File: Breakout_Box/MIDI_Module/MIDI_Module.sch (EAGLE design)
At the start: 71 parts, among them T1 2N2222, T2 2N2222, U1 TLV6004, U2 TLV6004, U3 MIC5205-5.0YM5-TR, U4 MIC5205-3.3YM5-TR

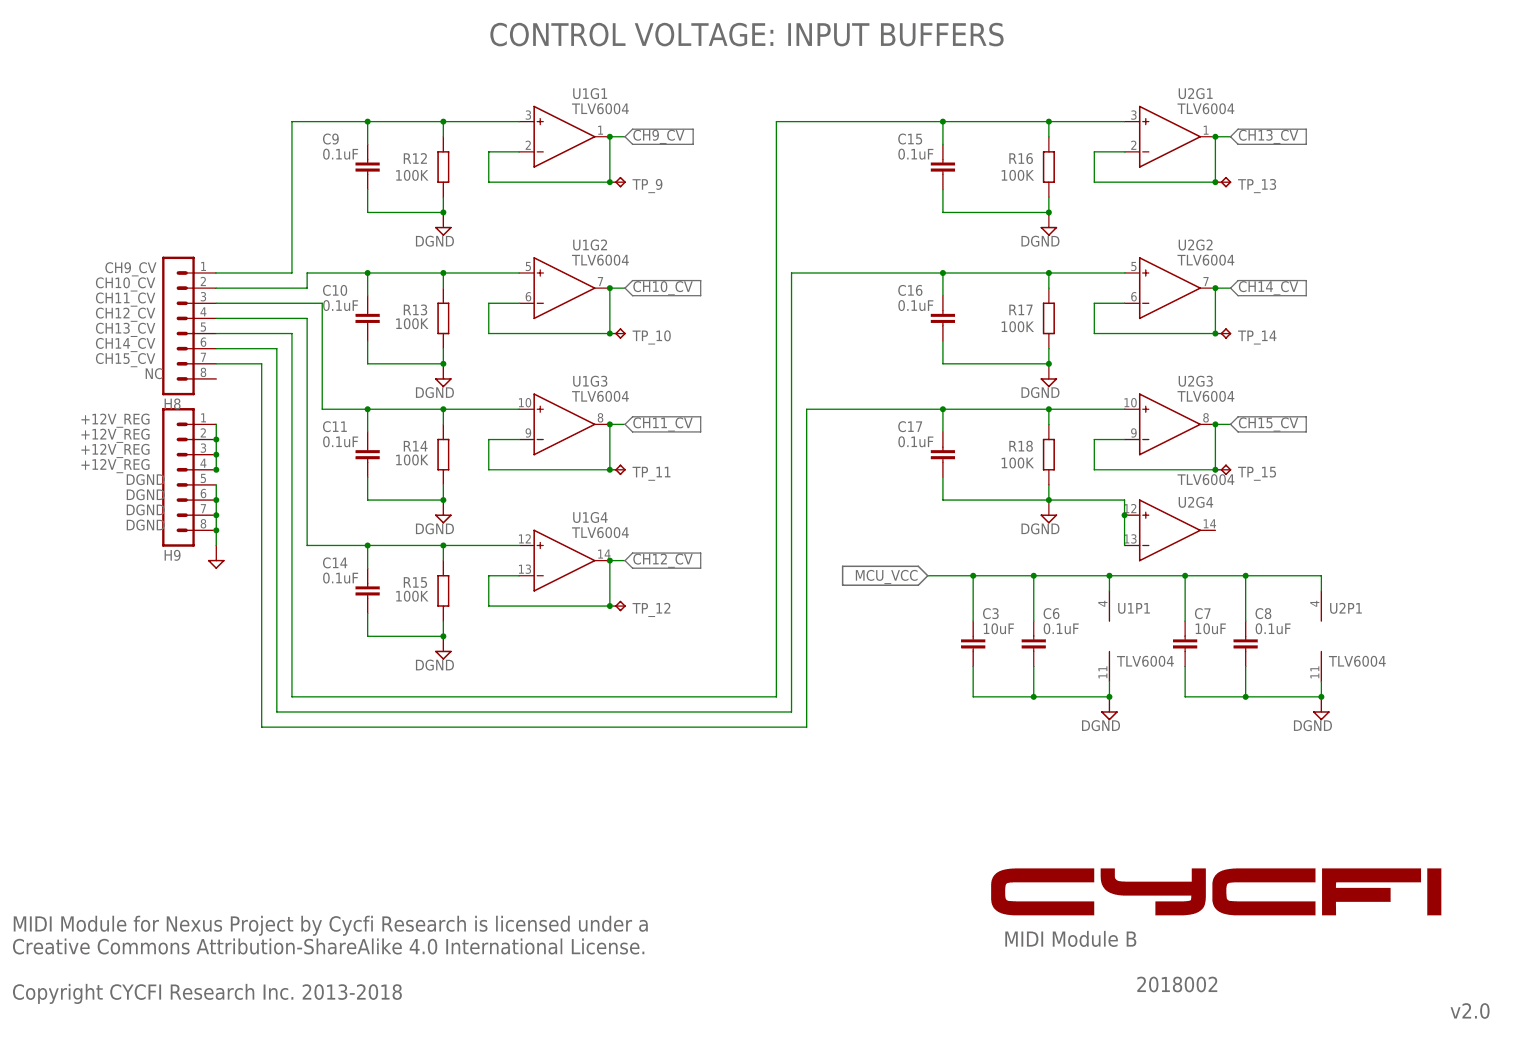
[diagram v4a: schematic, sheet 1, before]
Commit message: Update: Main Board MIDI Board MCU Board IO Board
Delete:
Mixer Board
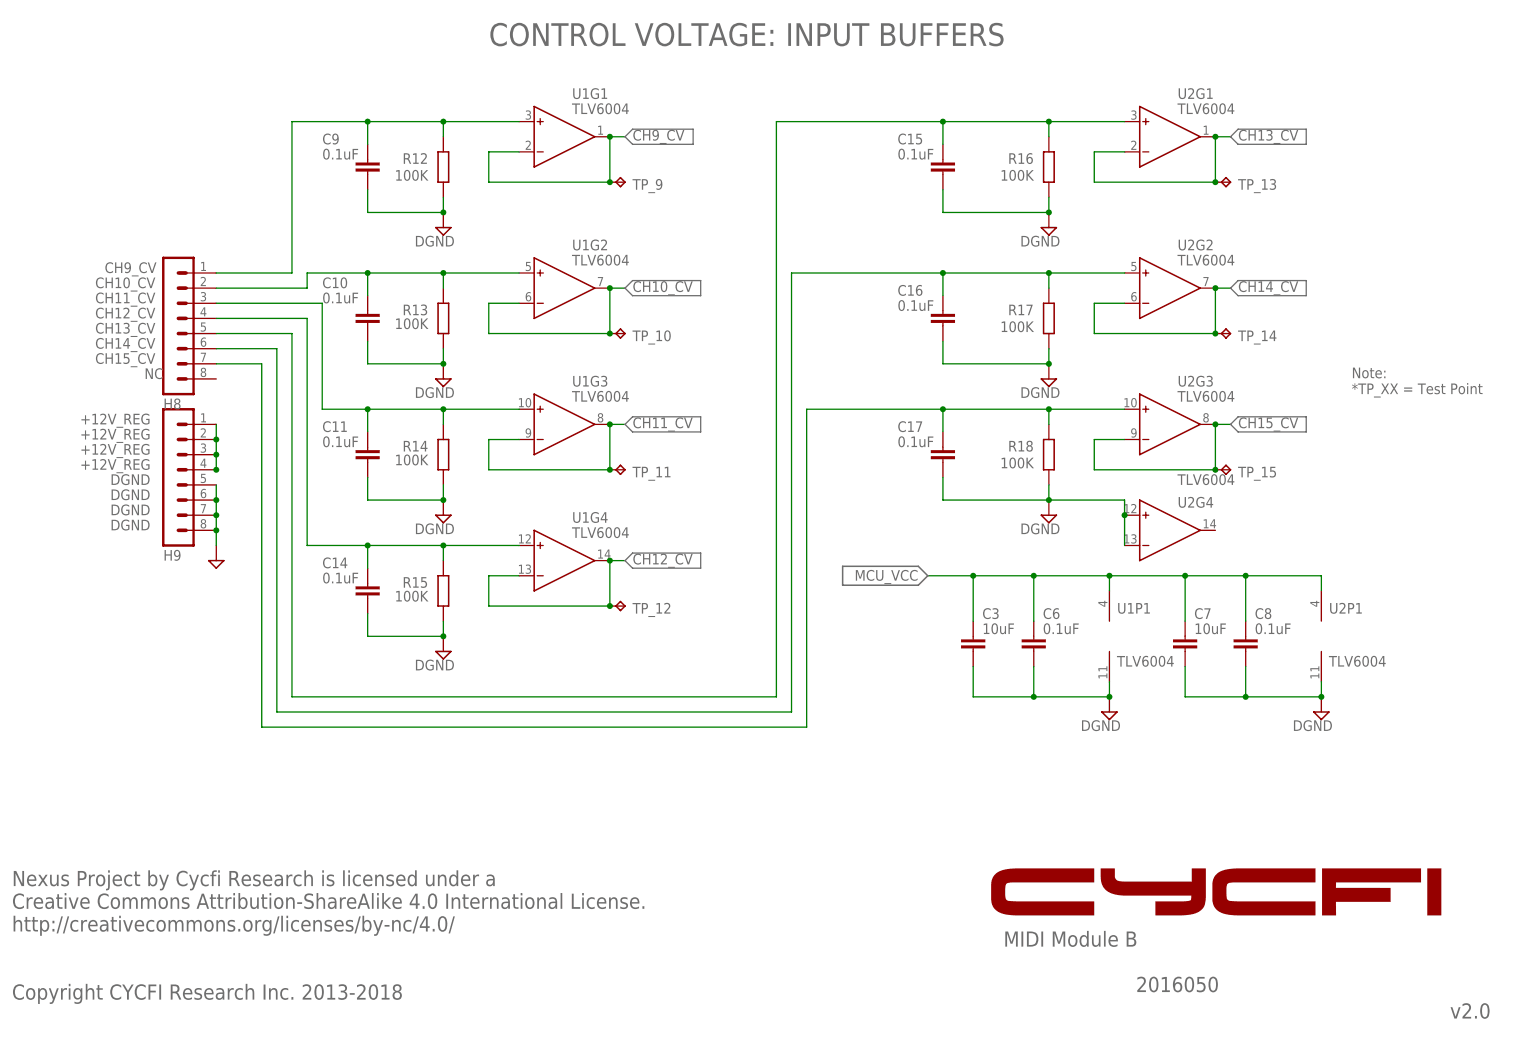
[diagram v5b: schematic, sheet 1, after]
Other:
- note added: "2016050"
- note added: "Nexus Project by Cycfi Research is licensed under a Creative Commons Attribution-ShareAlike 4.0 International License. http://creativecommons.org/licenses/by-nc/4.0/ Copyright CYCFI Research Inc. 2013-2018"
- note added: "Note: *TP_XX = Test Point"
- note removed: "2018002"
- note removed: "MIDI Module for Nexus Project by Cycfi Research is licensed under a Creative Commons Attribution-ShareAlike 4.0 International License. Copyright CYCFI Research Inc. 2013-2018"
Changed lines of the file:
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@@
 <setting verticaltext="up"/>
 </settings>
-<grid distance="0.1" unitdist="inch" unit="inch" style="lines" multiple="1" display="no" altdistance="0.01" altunitdist="inch" altunit="inch"/>
+<grid distance="0.05" unitdist="inch" unit="inch" style="lines" multiple="1" display="no" altdistance="0.01" altunitdist="inch" altunit="inch"/>
 <layers>
 <layer number="1" name="Top" color="4" fill="1" visible="no" active="no"/>
@@
 <text x="177.8" y="19.05" size="2.54" layer="95">MIDI Module B</text>
 <text x="252.73" y="6.985" size="2.54" layer="95">v2.0</text>
-<text x="200.025" y="11.43" size="2.54" layer="95">2018002</text>
+<text x="200.025" y="11.43" size="2.54" layer="95">2016050</text>
 <wire x1="150.8125" y1="82.8675" x2="150.8125" y2="79.6925" width="0.254" layer="95"/>
 <wire x1="150.8125" y1="79.6925" x2="163.5125" y2="79.6925" width="0.254" layer="95"/>
@@
 <text x="25.4" y="119.38" size="1.778" layer="95">CH14_CV</text>
 <text x="25.4" y="116.84" size="1.778" layer="95">CH15_CV</text>
-<text x="30.48" y="91.44" size="1.778" layer="95">DGND</text>
+<text x="27.94" y="91.44" size="1.778" layer="95">DGND</text>
 <text x="33.655" y="114.3" size="1.778" layer="95">NC</text>
 <wire x1="114.3" y1="154.94" x2="115.57" y2="153.67" width="0.1524" layer="95"/>
@@
 <wire x1="217.17" y1="156.21" x2="215.9" y2="154.94" width="0.1524" layer="95"/>
 <text x="91.44" y="170.18" size="3.81" layer="95">CONTROL VOLTAGE: INPUT BUFFERS</text>
-<text x="30.48" y="93.98" size="1.778" layer="95">DGND</text>
-<text x="30.48" y="96.52" size="1.778" layer="95">DGND</text>
-<text x="11.43" y="10.16" size="2.54" layer="95">MIDI Module for Nexus Project by Cycfi Research is licensed under a
+<text x="27.94" y="93.98" size="1.778" layer="95">DGND</text>
+<text x="27.94" y="96.52" size="1.778" layer="95">DGND</text>
+<text x="11.43" y="10.16" size="2.54" layer="95">Nexus Project by Cycfi Research is licensed under a
 Creative Commons Attribution-ShareAlike 4.0 International License.
+http://creativecommons.org/licenses/by-nc/4.0/
 Copyright CYCFI Research Inc. 2013-2018</text>
 <rectangle x1="179.80469375" y1="24.29065625" x2="193.0330125" y2="24.29954375" layer="94"/>
@@
 <rectangle x1="231.251125" y1="32.176084375" x2="247.86653125" y2="32.184971875" layer="94"/>
 <rectangle x1="248.915553125" y1="32.176084375" x2="251.271403125" y2="32.184971875" layer="94"/>
+<text x="236.22" y="111.76" size="1.778" layer="95">Note:
+*TP_XX = Test Point</text>
 </plain>
 <instances>
@@
 </instance>
 <instance part="C10" gate="G$1" x="71.12" y="125.73" smashed="yes">
-<attribute name="NAME" x="63.5" y="128.27" size="1.778" layer="95"/>
-<attribute name="VALUE" x="63.5" y="125.73" size="1.778" layer="96"/>
+<attribute name="NAME" x="63.5" y="129.54" size="1.778" layer="95"/>
+<attribute name="VALUE" x="63.5" y="127" size="1.778" layer="96"/>
 </instance>
 <instance part="C11" gate="G$1" x="71.12" y="102.87" smashed="yes">
@@
 <pinref part="H9" gate="1" pin="7"/>
 <wire x1="45.72" y1="91.44" x2="45.72" y2="88.9" width="0.1524" layer="91"/>
-<label x="30.48" y="88.9" size="1.778" layer="95"/>
+<label x="27.94" y="88.9" size="1.778" layer="95"/>
 <junction x="45.72" y="91.44"/>
 <pinref part="H9" gate="1" pin="5"/>
@@
 <text x="177.8" y="19.05" size="2.54" layer="95">MIDI Module A</text>
 <text x="252.73" y="6.985" size="2.54" layer="95">v2.0</text>
-<text x="200.025" y="11.43" size="2.54" layer="95">2018002</text>
+<text x="200.025" y="11.43" size="2.54" layer="95">2016050</text>
 <text x="142.24" y="122.555" size="1.778" layer="95" rot="MR0">P3.3</text>
 <text x="142.24" y="120.015" size="1.778" layer="95" rot="MR0">P3.2</text>
@@
 <wire x1="230.505" y1="96.52" x2="231.775" y2="96.52" width="0.1524" layer="94"/>
 <wire x1="214.63" y1="180.34" x2="214.63" y2="35.56" width="0.1524" layer="94" style="longdash"/>
-<text x="12.7" y="5.08" size="2.54" layer="95">MIDI Module for Nexus Project by Cycfi Research is licensed under a
+<text x="12.7" y="5.08" size="2.54" layer="95">Nexus Project by Cycfi Research is licensed under a
 Creative Commons Attribution-ShareAlike 4.0 International License.
+http://creativecommons.org/licenses/by-nc/4.0/
 Copyright CYCFI Research Inc. 2013-2018</text>
 <rectangle x1="179.80469375" y1="24.29065625" x2="193.0330125" y2="24.29954375" layer="94"/>
@@
 <wire x1="161.925" y1="143.51" x2="174.3075" y2="143.51" width="0.254" layer="95"/>
 <wire x1="174.3075" y1="143.51" x2="175.895" y2="145.0975" width="0.254" layer="95"/>
-<text x="200.025" y="11.43" size="2.54" layer="95">2018002</text>
+<text x="200.025" y="11.43" size="2.54" layer="95">2016050</text>
 <wire x1="172.085" y1="101.2825" x2="170.4975" y2="102.87" width="0.254" layer="95"/>
 <wire x1="170.4975" y1="102.87" x2="161.925" y2="102.87" width="0.254" layer="95"/>
@@
 <wire x1="86.36" y1="142.875" x2="101.6" y2="142.875" width="0.2032" layer="95"/>
 <wire x1="101.6" y1="142.875" x2="103.505" y2="144.78" width="0.2032" layer="95"/>
-<text x="12.7" y="16.51" size="2.54" layer="95">MIDI Module for Nexus Project by Cycfi Research is licensed under a
+<text x="12.7" y="16.51" size="2.54" layer="95">Nexus Project by Cycfi Research is licensed under a
 Creative Commons Attribution-ShareAlike 4.0 International License.
+http://creativecommons.org/licenses/by-nc/4.0/
 Copyright CYCFI Research Inc. 2013-2018</text>
 <rectangle x1="179.80469375" y1="24.29065625" x2="193.0330125" y2="24.29954375" layer="94"/>

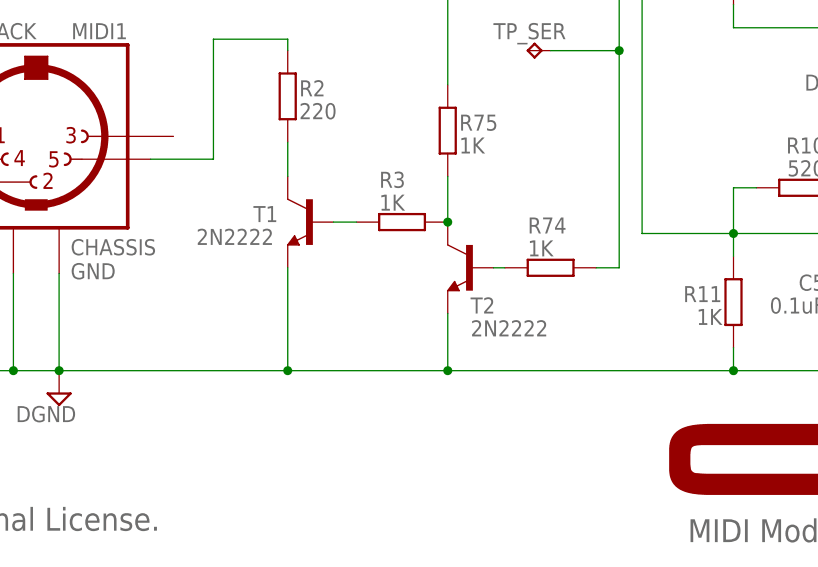
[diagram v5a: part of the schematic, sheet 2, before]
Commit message: Slight Changes to MIDI and MCU: - Change BJT Part number on MIDI_Module - Delete Ferrite Bead on MCU_Module
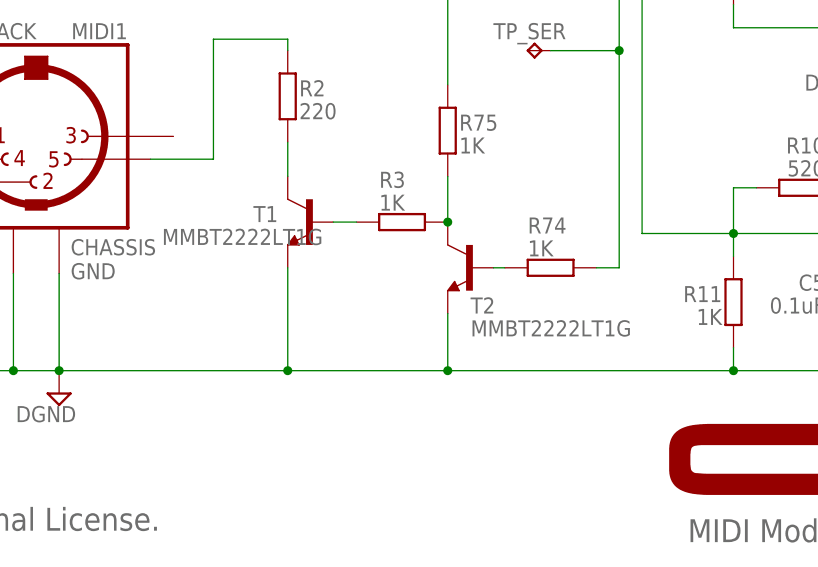
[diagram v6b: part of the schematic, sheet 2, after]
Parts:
- T1, T2: value 2N2222 -> MMBT2222LT1G
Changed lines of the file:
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@@
 <parts>
 <part name="FRAME1" library="frames" library_urn="urn:adsk.eagle:library:229" deviceset="DINA4_L" device=""/>
-<part name="T1" library="Cycfi" deviceset="TRAN-MMBT2222A" device="" value="2N2222"/>
+<part name="T1" library="Cycfi" deviceset="TRAN-MMBT2222A" device="" value="MMBT2222LT1G"/>
 <part name="R3" library="resistor" library_urn="urn:adsk.eagle:library:348" deviceset="R-EU_" device="R0402" package3d_urn="urn:adsk.eagle:package:26058/1" value="1K"/>
 <part name="R2" library="resistor" library_urn="urn:adsk.eagle:library:348" deviceset="R-EU_" device="R0402" package3d_urn="urn:adsk.eagle:package:26058/1" value="220"/>
@@
 <part name="C23" library="resistor" library_urn="urn:adsk.eagle:library:348" deviceset="C-EU" device="C0603" package3d_urn="urn:adsk.eagle:package:26138/1" value="0.1uF"/>
 <part name="C24" library="resistor" library_urn="urn:adsk.eagle:library:348" deviceset="C-EU" device="C0603" package3d_urn="urn:adsk.eagle:package:26138/1" value="0.1uF"/>
-<part name="T2" library="Cycfi" deviceset="TRAN-MMBT2222A" device="" value="2N2222"/>
+<part name="T2" library="Cycfi" deviceset="TRAN-MMBT2222A" device="" value="MMBT2222LT1G"/>
 <part name="R74" library="resistor" library_urn="urn:adsk.eagle:library:348" deviceset="R-EU_" device="R0402" package3d_urn="urn:adsk.eagle:package:26058/1" value="1K"/>
 <part name="R75" library="resistor" library_urn="urn:adsk.eagle:library:348" deviceset="R-EU_" device="R0402" package3d_urn="urn:adsk.eagle:package:26058/1" value="1K"/>
@@
 <instance part="T1" gate="G$1" x="135.89" y="54.61" smashed="yes" rot="MR0">
 <attribute name="NAME" x="129.54" y="54.61" size="1.778" layer="95"/>
-<attribute name="VALUE" x="123.19" y="52.07" size="1.778" layer="96"/>
+<attribute name="VALUE" x="119.38" y="52.07" size="1.778" layer="96"/>
 </instance>
 <instance part="R3" gate="G$1" x="146.05" y="54.61" smashed="yes" rot="MR0">
